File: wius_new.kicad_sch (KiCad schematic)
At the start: 0 parts

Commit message: insert of gpio expander
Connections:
- no-connect marks 4 -> 0
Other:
- sheet MCU ports: added EN_1V8, EN_1V8_GAP, LED_G, LED_R; removed none
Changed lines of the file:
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@@
 		(color 0 0 0 0)
 	)
-	(no_connect
-		(at 124.46 33.02)
-	)
-	(no_connect
-		(at 124.46 90.17)
-	)
-	(no_connect
-		(at 124.46 86.36)
-	)
-	(no_connect
-		(at 124.46 30.48)
-	)
 	(wire
 		(pts
@@
 		)
 	)
+	(wire
+		(pts
+			(xy 124.46 86.36) (xy 134.62 86.36)
+		)
+		(stroke
+			(width 0)
+			(type default)
+		)
+	)
 	(bus
 		(pts
@@
 		)
 	)
+	(wire
+		(pts
+			(xy 124.46 90.17) (xy 134.62 90.17)
+		)
+		(stroke
+			(width 0)
+			(type default)
+		)
+	)
 	(bus
 		(pts
@@
 		)
 	)
+	(wire
+		(pts
+			(xy 124.46 33.02) (xy 134.62 33.02)
+		)
+		(stroke
+			(width 0)
+			(type default)
+		)
+	)
 	(bus
 		(pts
@@
 		(pts
 			(xy 124.46 154.94) (xy 128.27 154.94)
+		)
+		(stroke
+			(width 0)
+			(type default)
+		)
+	)
+	(wire
+		(pts
+			(xy 124.46 30.48) (xy 134.62 30.48)
 		)
 		(stroke
@@
 			(effects
 				(font
+					(size 1.27 1.27)
+				)
+				(justify left)
+			)
+		)
+		(pin "LED_G" output
+			(at 134.62 30.48 180)
+			(effects
+				(font
+					(size 1.27 1.27)
+				)
+				(justify left)
+			)
+		)
+		(pin "LED_R" output
+			(at 134.62 33.02 180)
+			(effects
+				(font
+					(size 1.27 1.27)
+				)
+				(justify left)
+			)
+		)
+		(pin "EN_1V8" output
+			(at 134.62 90.17 180)
+			(effects
+				(font
+					(size 1.27 1.27)
+				)
+				(justify left)
+			)
+		)
+		(pin "EN_1V8_GAP" output
+			(at 134.62 86.36 180)
+			(effects
+				(font

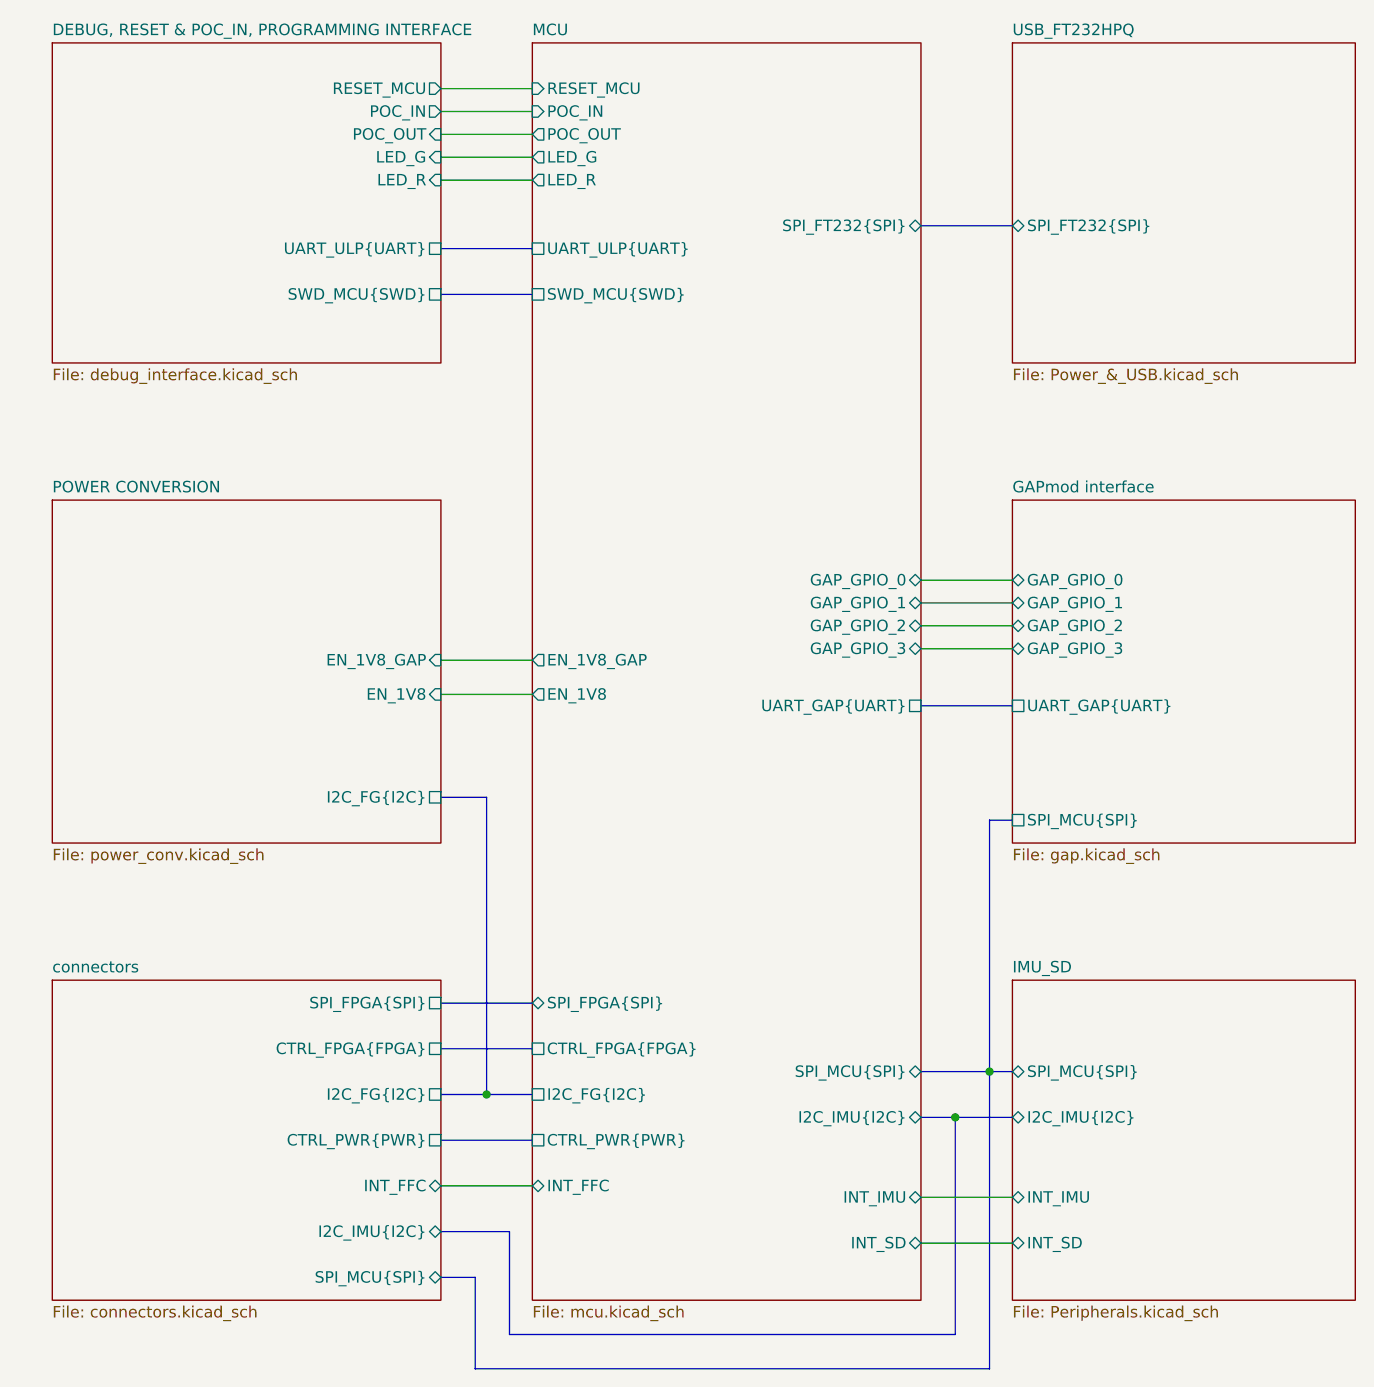
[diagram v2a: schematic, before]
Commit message: changes after first review: add lvl shifters, board at 1v8, new power tree
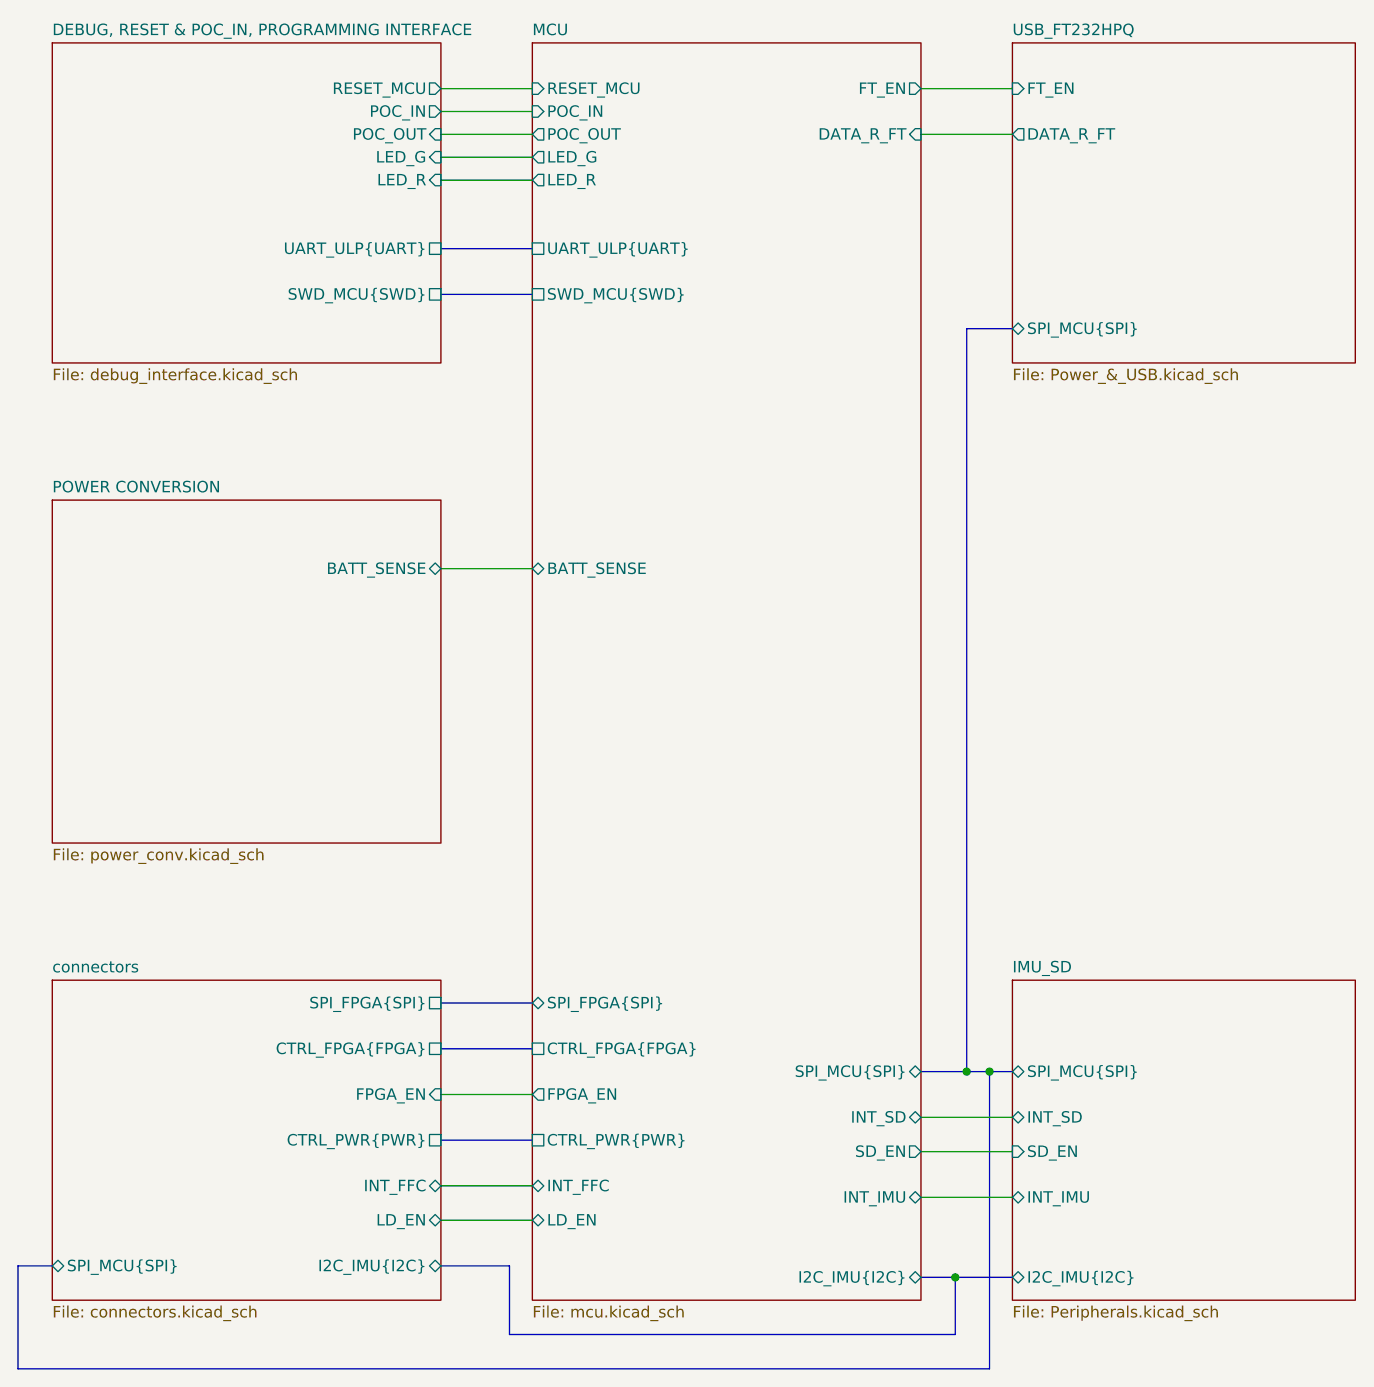
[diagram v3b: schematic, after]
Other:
- removed sheet GAPmod interface
- sheet IMU_SD ports: added SD_EN; removed none
- sheet MCU ports: added BATT_SENSE, DATA_R_FT, FPGA_EN, FT_EN, LD_EN, SD_EN; removed EN_1V8, EN_1V8_GAP, GAP_GPIO_0, GAP_GPIO_1, GAP_GPIO_2, GAP_GPIO_3, I2C_FG{I2C}, SPI_FT232{SPI}, UART_GAP{UART}
- sheet POWER CONVERSION ports: added BATT_SENSE; removed EN_1V8, EN_1V8_GAP, I2C_FG{I2C}
- sheet USB_FT232HPQ ports: added DATA_R_FT, FT_EN, SPI_MCU{SPI}; removed SPI_FT232{SPI}
- sheet connectors ports: added FPGA_EN, LD_EN; removed I2C_FG{I2C}

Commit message: updated schematic and initial pcb placement
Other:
- sheet MCU ports: added ULP_SSI{SPI}; removed LD_EN
- sheet connectors ports: added ULP_SSI{SPI}; removed LD_EN, SPI_MCU{SPI}
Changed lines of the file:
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@@
 		(color 0 0 0 0)
 	)
-	(junction
-		(at 185.42 132.08)
-		(diameter 0)
-		(color 0 0 0 0)
-	)
 	(bus
 		(pts
@@
 	(bus
 		(pts
-			(xy 77.47 165.1) (xy 185.42 165.1)
-		)
-		(stroke
-			(width 0)
-			(type default)
-		)
-	)
-	(bus
-		(pts
-			(xy 182.88 132.08) (xy 185.42 132.08)
+			(xy 182.88 132.08) (xy 187.96 132.08)
 		)
 		(stroke
@@
 	(bus
 		(pts
+			(xy 77.47 119.38) (xy 134.62 119.38)
+		)
+		(stroke
+			(width 0)
+			(type default)
+		)
+	)
+	(bus
+		(pts
+			(xy 81.28 124.46) (xy 77.47 124.46)
+		)
+		(stroke
+			(width 0)
+			(type default)
+		)
+	)
+	(bus
+		(pts
+			(xy 77.47 119.38) (xy 77.47 124.46)
+		)
+		(stroke
+			(width 0)
+			(type default)
+		)
+	)
+	(bus
+		(pts
 			(xy 124.46 124.46) (xy 134.62 124.46)
 		)
@@
 	(bus
 		(pts
-			(xy 185.42 165.1) (xy 185.42 132.08)
-		)
-		(stroke
-			(width 0)
-			(type default)
-		)
-	)
-	(bus
-		(pts
-			(xy 77.47 153.67) (xy 81.28 153.67)
-		)
-		(stroke
-			(width 0)
-			(type default)
-		)
-	)
-	(bus
-		(pts
 			(xy 181.61 154.94) (xy 181.61 161.29)
 		)
@@
 	(bus
 		(pts
-			(xy 185.42 132.08) (xy 187.96 132.08)
-		)
-		(stroke
-			(width 0)
-			(type default)
-		)
-	)
-	(bus
-		(pts
 			(xy 181.61 154.94) (xy 187.96 154.94)
 		)
@@
 		(pts
 			(xy 124.46 30.48) (xy 134.62 30.48)
-		)
-		(stroke
-			(width 0)
-			(type default)
-		)
-	)
-	(wire
-		(pts
-			(xy 124.46 148.59) (xy 134.62 148.59)
-		)
-		(stroke
-			(width 0)
-			(type default)
-		)
-	)
-	(bus
-		(pts
-			(xy 77.47 165.1) (xy 77.47 153.67)
 		)
 		(stroke
@@
 			)
 		)
-		(pin "LD_EN" bidirectional
-			(at 134.62 148.59 180)
-			(effects
-				(font
-					(size 1.27 1.27)
-				)
-				(justify left)
-			)
-		)
 		(pin "SD_EN" output
 			(at 177.8 140.97 0)
@@
 		(pin "BATT_SENSE" bidirectional
 			(at 134.62 76.2 180)
+			(effects
+				(font
+					(size 1.27 1.27)
+				)
+				(justify left)
+			)
+		)
+		(pin "ULP_SSI{SPI}" bidirectional
+			(at 134.62 119.38 180)
 			(effects
 				(font
@@
 			)
 		)
-		(pin "SPI_MCU{SPI}" bidirectional
-			(at 81.28 153.67 180)
-			(effects
-				(font
-					(size 1.27 1.27)
-				)
-				(justify left)
-			)
-		)
 		(pin "FPGA_EN" input
 			(at 124.46 134.62 0)
@@
 			)
 		)
-		(pin "LD_EN" bidirectional
-			(at 124.46 148.59 0)
-			(effects
-				(font
-					(size 1.27 1.27)
-				)
-				(justify right)
-			)
-		)
+		(pin "ULP_SSI{SPI}" bidirectional
+			(at 81.28 124.46 180)
+			(effects
+				(font
+					(size 1.27 1.27)
+				)
+				(justify left)
+			)
+		)
